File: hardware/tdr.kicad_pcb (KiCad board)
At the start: 4 copper layers, 98.8 x 47 mm, 238 parts, among them J201 Conn_02x01, J202 Conn_Coaxial, J203 Conn_Coaxial, J204 Conn_Coaxial, J205 Conn_Coaxial, J207 Conn_Coaxial, J208 Conn_Coaxial, J209 Conn_Coaxial, J210 Barrel_Jack_Switch, J801 Conn_02x06_Counter_Clockwise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

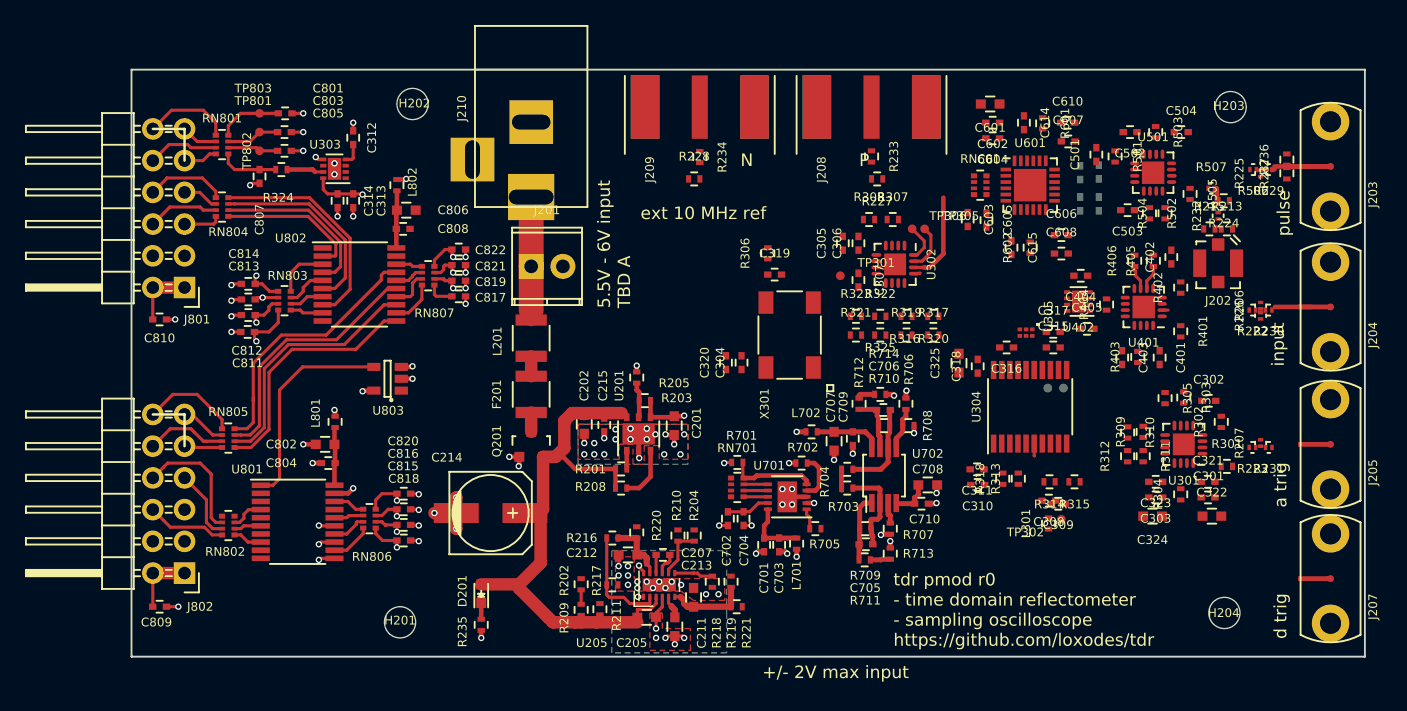
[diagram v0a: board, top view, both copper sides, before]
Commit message: routing high speed digital
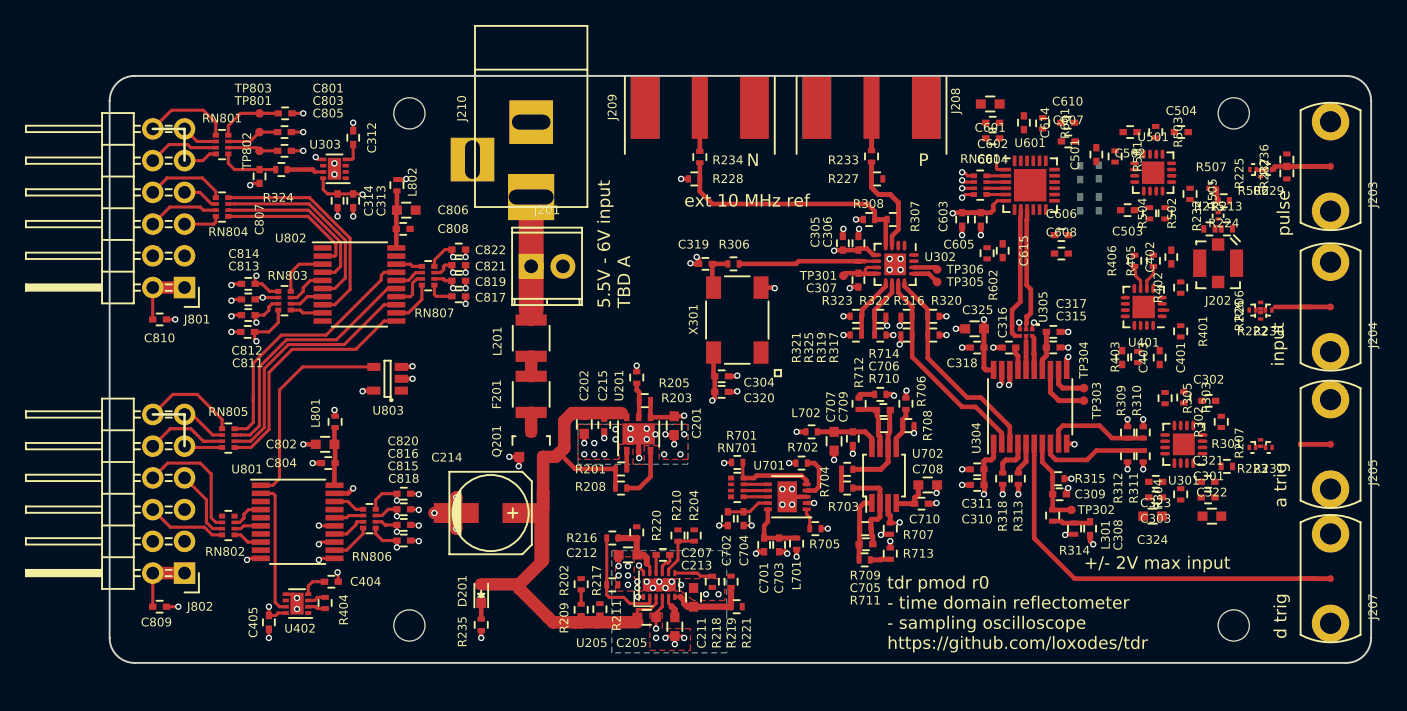
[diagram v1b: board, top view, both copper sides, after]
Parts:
- TP303, TP304: moved to F.Cu
- moved C405 69.6 mm to (101.8, 102.8), turned to 270 degrees
- moved U402 67.1 mm to (104.0, 101.2)
- moved R404 67.0 mm to (106.2, 101.2)
- moved C404 64.8 mm to (106.8, 99.5), turned to 0 degrees
- moved C319 5.61 mm to (136.7, 74.0), turned to 180 degrees
- moved TP305 4.37 mm to (155.2, 75.5)
- moved X301 4.36 mm to (139.2, 78.5)
- moved C308 3.99 mm to (167.5, 95.2), turned to 270 degrees
- moved TP306 3.82 mm to (155.2, 74.5)
- moved R602 3.48 mm to (159.2, 73.2)
- moved TP303 3.06 mm to (167.0, 85.0), turned to 270 degrees
- moved C325 3.02 mm to (158.2, 79.2), turned to 180 degrees
- moved R306 2.87 mm to (138.9, 74.0), turned to 0 degrees
- moved R314 2.71 mm to (164.5, 94.2), turned to 90 degrees
- moved C320 2.37 mm to (138.0, 84.3), turned to 0 degrees
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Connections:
- U302 pad 13: /CLK_PULSE_P -> Net-(TP305-Pad1)
- U302 pad 14: /CLK_PULSE_N -> Net-(TP306-Pad1)
- U302 pad 15: Net-(TP305-Pad1) -> /CLK_PULSE_P
- U302 pad 16: Net-(TP306-Pad1) -> /CLK_PULSE_N
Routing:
- net +3V3: track 12.2 -> 48.9 mm, vias 6 -> 21
- net /EXT_TRIG: track 0.98 -> 31.3 mm
- net GND: track 52.1 -> 77.1 mm, vias 94 -> 134
- net /EXT_CLK_N: track 0.00 -> 20.8 mm
- net Net-(R317-Pad1): track 0.00 -> 17.0 mm
- net Net-(R316-Pad1): track 0.00 -> 16.9 mm
- net Net-(R306-Pad2): track 0.00 -> 11.8 mm
- net /CLK_SAMPLE_N: track 0.00 -> 11.0 mm
- net /COMPARATOR_OUTPUT: track 0.00 -> 10.8 mm
- net /CLK_SAMPLE_P: track 0.00 -> 9.96 mm
- net Net-(R311-Pad1): track 0.00 -> 8.79 mm
- net Net-(R309-Pad1): track 0.00 -> 8.45 mm
- net /EXT_CLK_P: track 0.00 -> 8.35 mm
- net Net-(C309-Pad1): track 0.00 -> 7.15 mm
- net /CLK_PULSE_N: track 7.31 -> 0.25 mm
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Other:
- board size 98.8 x 47 mm -> 101 x 47 mm

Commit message: more layout.. 28 unrouted nets to go
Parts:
- added C326: 100 pF, Capacitors_SMD:C_0402, F.Cu at (179.2, 86.5)
- added G***: LOGO, vna_footprints:cat, B.Cu at (120.5, 82.0)
- C601, C602: moved to B.Cu
- J208, J209: footprint vna_footprints:732511150_sma_thin -> vna_footprints:732511150_sma_thin_twopin
- moved C604 1.99 mm to (158.8, 65.8)
- moved C601 1.82 mm to (160.0, 63.0), turned to 0 degrees
- moved C602 1.75 mm to (159.8, 64.5), turned to 0 degrees
- moved C608 0.62 mm to (164.8, 72.8)
- moved C614 0.59 mm to (162.8, 63.0)
- moved C403 0.53 mm to (170.5, 81.2)
- moved R403 0.50 mm to (171.8, 81.2)
- moved C606 0.47 mm to (164.8, 71.5)
- moved R236 0.43 mm to (183.5, 66.0)
- moved R601 0.39 mm to (164.0, 63.0)
- moved R232 0.32 mm to (177.5, 70.0)
- moved C401 0.30 mm to (173.1, 81.2)
- moved R237 0.29 mm to (183.0, 67.0)
- moved C610 0.27 mm to (165.8, 63.0)
- moved C501 0.27 mm to (168.2, 65.2)
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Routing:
- net +3V3: track 48.9 -> 263.6 mm, vias 21 -> 27
- net +5VA: track 1.35 -> 139.4 mm, vias 2 -> 9
- net -5VA: track 3.16 -> 111.8 mm, vias 0 -> 6
- net GND: track 77.1 -> 162.7 mm, vias 134 -> 214
- net /sheet5C262FB0/DAC_VOUT: track 1.62 -> 58.6 mm, vias 0 -> 2
- net /ANALOG_TRIG_LEVEL: track 1.64 -> 57.0 mm, vias 0 -> 2
- net /PGOOD_3V3: track 5.27 -> 41.9 mm, vias 1 -> 2
- net Net-(R706-Pad2): track 1.22 -> 15.9 mm
- net /sheet5C262FB0/DAC_VREF: track 5.29 -> 18.2 mm, vias 0 -> 2
- net /~LATCH: track 0.00 -> 10.3 mm
- net Net-(R206-Pad2): track 0.00 -> 9.89 mm
- net Net-(R207-Pad2): track 0.00 -> 9.54 mm
- net Net-(C615-Pad1): track 0.00 -> 8.03 mm, vias 0 -> 2
- net VPP: track 53.5 -> 61.4 mm, vias 0 -> 2
- net /LATCH: track 0.00 -> 7.95 mm
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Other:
- board text added: "5.5V - 6V input"
- board text removed: "5.5V - 6V input TBD A"

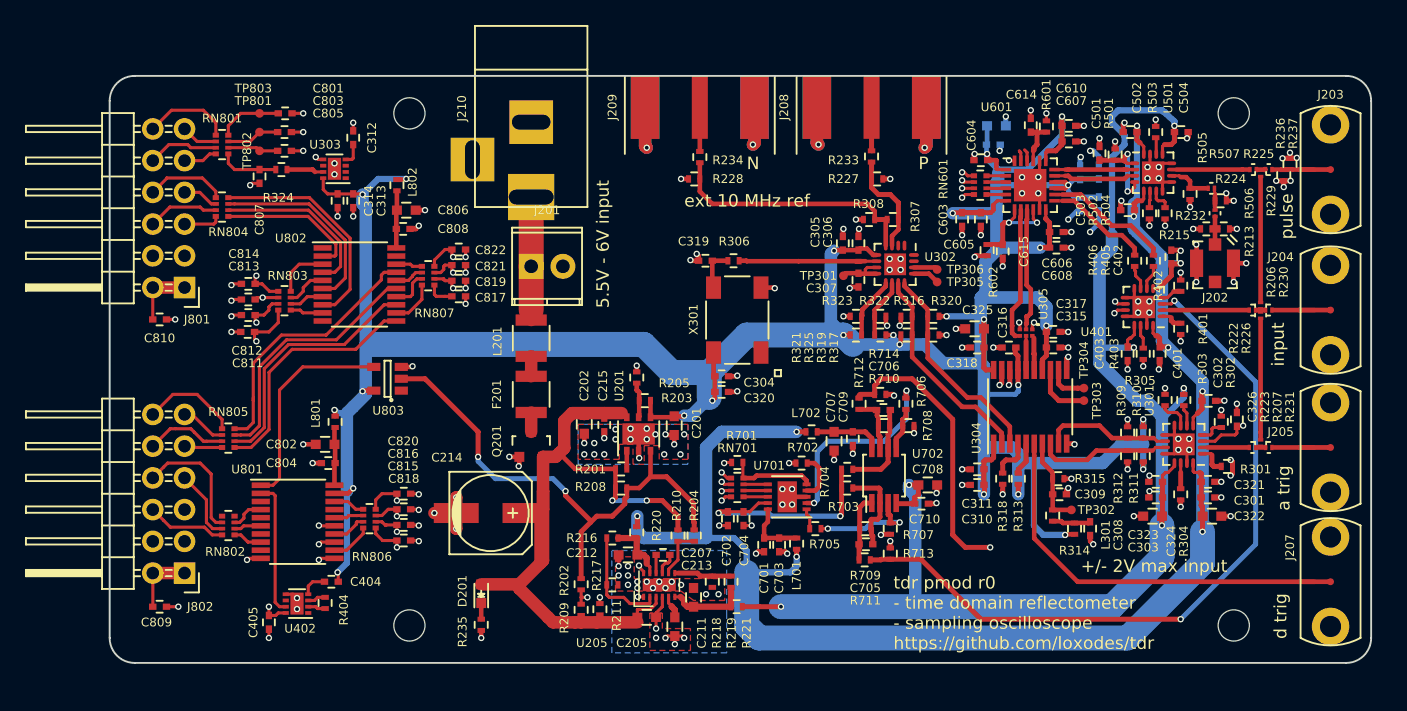
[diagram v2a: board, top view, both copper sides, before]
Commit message: first pass of layout complete
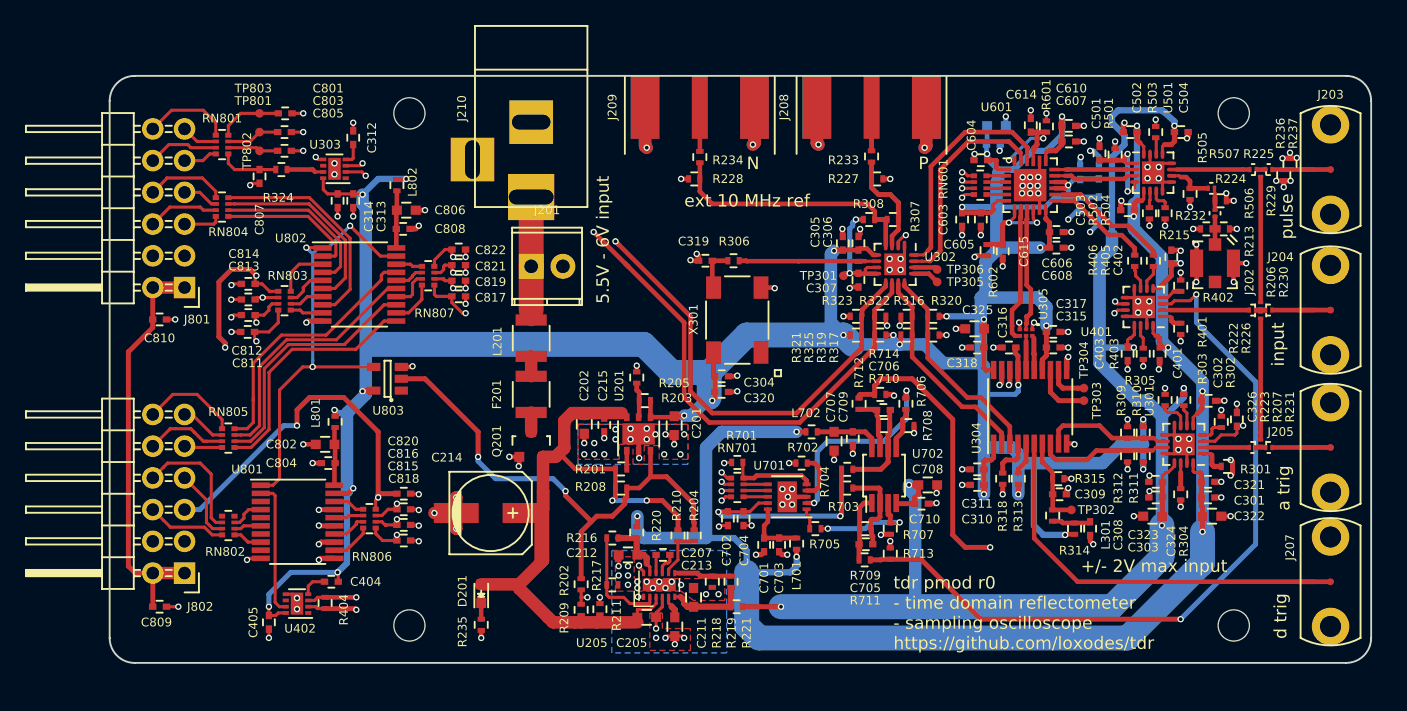
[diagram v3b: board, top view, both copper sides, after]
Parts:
- U303, U402: footprint Housings_DFN_QFN:DFN-8-1EP_2x2mm_Pitch0.5mm -> vna_footprints:DFN-8-1EP_2x2mm_Pitch0.5mm
- moved G*** 5.32 mm to (117.0, 86.0)
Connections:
- C815 pad 1: /fpga_connector/DELAY_~EN -> /fpga_connector/DAC_SDI
- C816 pad 1: /fpga_connector/DELAY_SCLK -> /fpga_connector/DAC_SCK
- C817 pad 1: /fpga_connector/DAC_SDI -> /fpga_connector/DAC_~CLR
- C818 pad 1: /fpga_connector/DELAY_SDIN -> /fpga_connector/DAC_CS
- C819 pad 1: /fpga_connector/DAC_SCK -> /fpga_connector/DELAY_SCLK
- C821 pad 1: /fpga_connector/DAC_CS -> /fpga_connector/DELAY_SDIN
- C822 pad 1: /fpga_connector/DAC_~CLR -> /fpga_connector/DELAY_~EN
- RN806 pad 5: /fpga_connector/DELAY_~EN -> /fpga_connector/DAC_SDI
- RN806 pad 6: /fpga_connector/DELAY_SCLK -> /fpga_connector/DAC_SCK
- RN806 pad 7: /fpga_connector/DELAY_SDIN -> /fpga_connector/DAC_CS
- RN807 pad 5: /fpga_connector/DAC_SDI -> /fpga_connector/DAC_~CLR
- RN807 pad 6: /fpga_connector/DAC_SCK -> /fpga_connector/DELAY_SCLK
- RN807 pad 7: /fpga_connector/DAC_CS -> /fpga_connector/DELAY_SDIN
- RN807 pad 8: /fpga_connector/DAC_~CLR -> /fpga_connector/DELAY_~EN
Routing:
- net /fpga_connector/DELAY_SLOAD: track 5.03 -> 108.8 mm
- net /clock/CLK_SEL: track 3.01 -> 101.5 mm, vias 1 -> 2
- net /fpga_connector/SEL1: track 4.07 -> 97.7 mm, vias 2 -> 3
- net /fpga_connector/SEL0: track 3.15 -> 96.5 mm
- net Net-(R404-Pad1): track 2.38 -> 86.8 mm, vias 1 -> 2
- net Net-(R404-Pad2): track 2.35 -> 85.8 mm, vias 1 -> 2
- net Net-(R322-Pad1): track 4.74 -> 63.3 mm, vias 0 -> 2
- net Net-(R321-Pad2): track 4.97 -> 62.1 mm, vias 0 -> 2
- net /fpga_connector/DELAY_~EN: track 3.99 -> 50.2 mm
- net /fpga_connector/DELAY_SDIN: track 3.41 -> 48.9 mm
- net /fpga_connector/DELAY_SCLK: track 3.45 -> 48.2 mm
- net /fpga_connector/DAC_SDI: track 3.09 -> 33.1 mm, vias 1 -> 2
- net /fpga_connector/DAC_SCK: track 2.90 -> 32.7 mm
- net /fpga_connector/DAC_~CLR: track 3.83 -> 32.8 mm
- net /fpga_connector/DAC_CS: track 3.34 -> 31.2 mm
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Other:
- rule trace_min: 0.127 -> 0.13
